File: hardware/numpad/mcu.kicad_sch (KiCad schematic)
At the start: 7 parts, among them U1 STM32L011F4Px

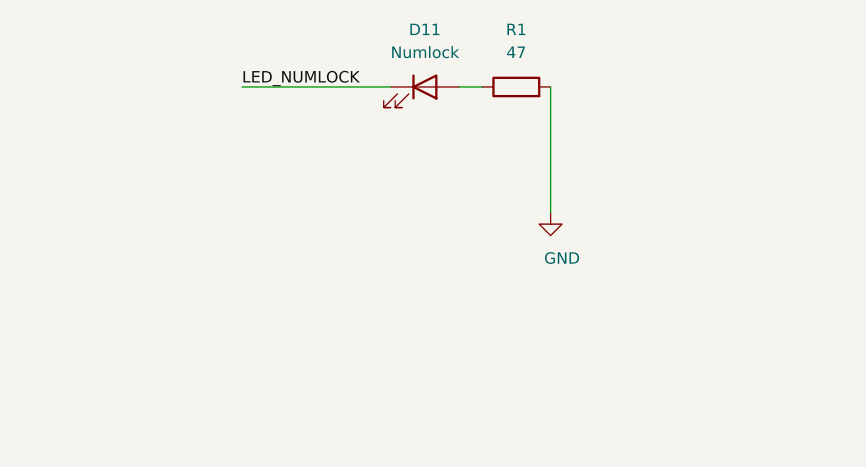
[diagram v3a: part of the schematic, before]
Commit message: Numpad: Add break-away board with the numpad LED
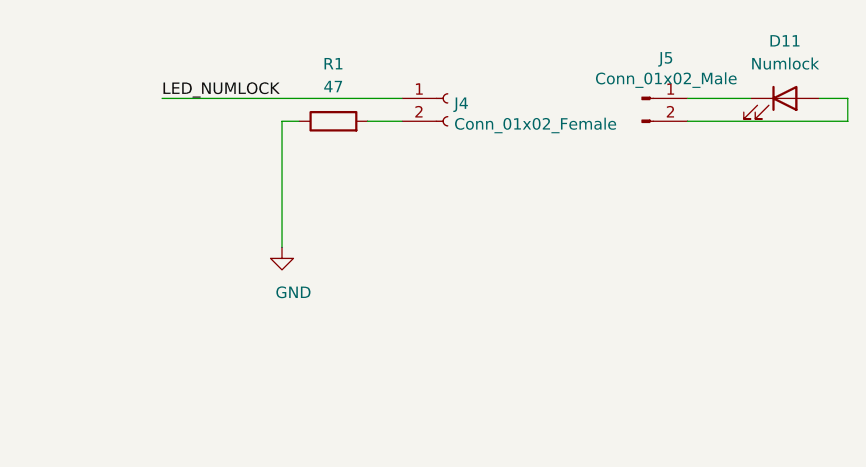
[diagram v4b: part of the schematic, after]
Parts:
- added J4: Conn_01x02_Female, Connector_PinHeader_2.54mm:PinHeader_1x02_P2.54mm_Vertical, symbol Connector:Conn_01x02_Female
- added J5: Conn_01x02_Male, Connector_PinHeader_2.54mm:PinHeader_1x02_P2.54mm_Vertical, symbol Connector:Conn_01x02_Male
- D11: footprint Diode_THT:D_DO-34_SOD68_P2.54mm_Vertical_AnodeUp -> Diode_SMD:D_0603_1608Metric_Pad1.05x0.95mm_HandSolder; Mouser (none) -> 710-150060SS75000; Part Name (none) -> 150060SS75000
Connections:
- net GND: now also R1.1; no longer R1.2
- net LED_NUMLOCK: now also J4.1 (Pin_1); no longer D11.1 (K)
- net at D11.2 (A): now also J5.2 (Pin_2); no longer R1.1
- new net: D11.1 (K), J5.1 (Pin_1)
- new net: J4.2 (Pin_2), R1.2
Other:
- moved on the sheet: D11, R1
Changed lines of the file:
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@@
     (stroke (width 0) (type solid) (color 0 0 0 0))
   )
-  (wire (pts (xy 200.66 54.61) (xy 217.17 54.61))
+  (wire (pts (xy 191.77 55.88) (xy 218.44 55.88))
     (stroke (width 0) (type solid) (color 0 0 0 0))
   )
-  (wire (pts (xy 224.79 54.61) (xy 227.33 54.61))
+  (wire (pts (xy 205.105 58.42) (xy 205.105 72.39))
     (stroke (width 0) (type solid) (color 0 0 0 0))
   )
-  (wire (pts (xy 234.95 54.61) (xy 234.95 68.58))
+  (wire (pts (xy 205.105 58.42) (xy 207.01 58.42))
+    (stroke (width 0) (type solid) (color 0 0 0 0))
+  )
+  (wire (pts (xy 214.63 58.42) (xy 218.44 58.42))
+    (stroke (width 0) (type solid) (color 0 0 0 0))
+  )
+  (wire (pts (xy 250.19 55.88) (xy 257.175 55.88))
+    (stroke (width 0) (type solid) (color 0 0 0 0))
+  )
+  (wire (pts (xy 250.19 58.42) (xy 267.97 58.42))
+    (stroke (width 0) (type solid) (color 0 0 0 0))
+  )
+  (wire (pts (xy 264.795 55.88) (xy 267.97 55.88))
+    (stroke (width 0) (type solid) (color 0 0 0 0))
+  )
+  (wire (pts (xy 267.97 58.42) (xy 267.97 55.88))
     (stroke (width 0) (type solid) (color 0 0 0 0))
   )
@@
     (effects (font (size 1.27 1.27)) (justify right bottom))
   )
-  (label "LED_NUMLOCK" (at 200.66 54.61 0)
+  (label "LED_NUMLOCK" (at 191.77 55.88 0)
     (effects (font (size 1.27 1.27)) (justify left bottom))
   )
@@
     (pin "1")
   )
-  (symbol (lib_id "power:GND") (at 234.95 68.58 0) (unit 1)
+  (symbol (lib_id "power:GND") (at 205.105 72.39 0) (unit 1)
     (in_bom yes) (on_board yes)
-    (property "Reference" "#PWR0112" (id 0) (at 234.95 74.93 0)
+    (property "Reference" "#PWR0112" (id 0) (at 205.105 78.74 0)
       (effects (font (size 1.27 1.27)) hide)
     )
-    (property "Value" "GND" (id 1) (at 236.22 73.66 0))
-    (property "Footprint" "" (id 2) (at 234.95 68.58 0)
+    (property "Value" "GND" (id 1) (at 206.375 77.47 0))
+    (property "Footprint" "" (id 2) (at 205.105 72.39 0)
       (effects (font (size 1.27 1.27)) hide)
     )
-    (property "Datasheet" "" (id 3) (at 234.95 68.58 0)
+    (property "Datasheet" "" (id 3) (at 205.105 72.39 0)
       (effects (font (size 1.27 1.27)) hide)
     )
     (pin "1")
   )
-  (symbol (lib_id "Device:R") (at 231.14 54.61 90) (unit 1)
+  (symbol (lib_id "Device:R") (at 210.82 58.42 90) (unit 1)
     (in_bom yes) (on_board yes)
-    (property "Reference" "R1" (id 0) (at 231.14 48.26 90))
-    (property "Value" "47" (id 1) (at 231.14 50.8 90))
-    (property "Footprint" "Resistor_SMD:R_0603_1608Metric_Pad0.98x0.95mm_HandSolder" (id 2) (at 231.14 56.388 90)
+    (property "Reference" "R1" (id 0) (at 210.82 52.07 90))
+    (property "Value" "47" (id 1) (at 210.82 54.61 90))
+    (property "Footprint" "Resistor_SMD:R_0603_1608Metric_Pad0.98x0.95mm_HandSolder" (id 2) (at 210.82 60.198 90)
       (effects (font (size 1.27 1.27)) hide)
     )
-    (property "Datasheet" "~" (id 3) (at 231.14 54.61 0)
+    (property "Datasheet" "~" (id 3) (at 210.82 58.42 0)
       (effects (font (size 1.27 1.27)) hide)
     )
@@
     (pin "2")
   )
-  (symbol (lib_id "Device:LED") (at 220.98 54.61 0) (unit 1)
+  (symbol (lib_id "Connector:Conn_01x02_Male") (at 245.11 55.88 0) (unit 1)
     (in_bom yes) (on_board yes)
-    (property "Reference" "D11" (id 0) (at 220.98 48.26 0))
-    (property "Value" "Numlock" (id 1) (at 220.98 50.8 0))
-    (property "Footprint" "Diode_THT:D_DO-34_SOD68_P2.54mm_Vertical_AnodeUp" (id 2) (at 220.98 54.61 0)
+    (property "Reference" "J5" (id 0) (at 247.8024 51.4158 0))
+    (property "Value" "Conn_01x02_Male" (id 1) (at 247.8024 53.7145 0))
+    (property "Footprint" "Connector_PinHeader_2.54mm:PinHeader_1x02_P2.54mm_Vertical" (id 2) (at 245.11 55.88 0)
       (effects (font (size 1.27 1.27)) hide)
     )
-    (property "Datasheet" "~" (id 3) (at 220.98 54.61 0)
+    (property "Datasheet" "~" (id 3) (at 245.11 55.88 0)
       (effects (font (size 1.27 1.27)) hide)
     )
+    (pin "1")
+    (pin "2")
+  )
+  (symbol (lib_id "Connector:Conn_01x02_Female") (at 223.52 55.88 0) (unit 1)
+    (in_bom yes) (on_board yes)
+    (property "Reference" "J4" (id 0) (at 224.2313 56.4578 0)
+      (effects (font (size 1.27 1.27)) (justify left))
+    )
+    (property "Value" "Conn_01x02_Female" (id 1) (at 224.2313 58.7565 0)
+      (effects (font (size 1.27 1.27)) (justify left))
+    )
+    (property "Footprint" "Connector_PinHeader_2.54mm:PinHeader_1x02_P2.54mm_Vertical" (id 2) (at 223.52 55.88 0)
+      (effects (font (size 1.27 1.27)) hide)
+    )
+    (property "Datasheet" "~" (id 3) (at 223.52 55.88 0)
+      (effects (font (size 1.27 1.27)) hide)
+    )
+    (pin "1")
+    (pin "2")
+  )
+  (symbol (lib_id "Device:LED") (at 260.985 55.88 0) (unit 1)
+    (in_bom yes) (on_board yes)
+    (property "Reference" "D11" (id 0) (at 260.985 49.53 0))
+    (property "Value" "Numlock" (id 1) (at 260.985 52.07 0))
+    (property "Footprint" "Diode_SMD:D_0603_1608Metric_Pad1.05x0.95mm_HandSolder" (id 2) (at 260.985 55.88 0)
+      (effects (font (size 1.27 1.27)) hide)
+    )
+    (property "Datasheet" "~" (id 3) (at 260.985 55.88 0)
+      (effects (font (size 1.27 1.27)) hide)
+    )
+    (property "Mouser" "710-150060SS75000" (id 4) (at 260.985 55.88 0)
+      (effects (font (size 1.27 1.27)) hide)
+    )
+    (property "Part Name" "150060SS75000 " (id 5) (at 260.985 55.88 0)
+      (effects (font (size 1.27 1.27)) hide)
+    )

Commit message: Numpad: Exchange footprint of the numpad-LED connection
The 2.54 mm pin-header did not fit between the switches as the
silkscreens overlapped.
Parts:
- J4, J5: footprint Connector_PinHeader_2.54mm:PinHeader_1x02_P2.54mm_Vertical -> Connector_PinSocket_2.00mm:PinSocket_1x02_P2.00mm_Vertical
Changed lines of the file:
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@@
     (property "Reference" "J5" (id 0) (at 247.8024 51.4158 0))
     (property "Value" "Conn_01x02_Male" (id 1) (at 247.8024 53.7145 0))
-    (property "Footprint" "Connector_PinHeader_2.54mm:PinHeader_1x02_P2.54mm_Vertical" (id 2) (at 245.11 55.88 0)
+    (property "Footprint" "Connector_PinSocket_2.00mm:PinSocket_1x02_P2.00mm_Vertical" (id 2) (at 245.11 55.88 0)
       (effects (font (size 1.27 1.27)) hide)
     )
@@
       (effects (font (size 1.27 1.27)) (justify left))
     )
-    (property "Footprint" "Connector_PinHeader_2.54mm:PinHeader_1x02_P2.54mm_Vertical" (id 2) (at 223.52 55.88 0)
+    (property "Footprint" "Connector_PinSocket_2.00mm:PinSocket_1x02_P2.00mm_Vertical" (id 2) (at 223.52 55.88 0)
       (effects (font (size 1.27 1.27)) hide)
     )

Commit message: Numpad: Add missing part numbers
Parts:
- C2, C4: Mouser (none) -> 581-06033C104KAT4A; Part Name (none) -> AVX 06033C104KAT4A
- C3, C5: footprint Capacitor_SMD:C_0603_1608Metric_Pad1.08x0.95mm_HandSolder -> Capacitor_SMD:C_0805_2012Metric; Mouser (none) -> 187-CL21A106KOQNNNG; Part Name (none) -> Samsung CL21A106KOQNNNG
- J4, J5: Mouser (none) -> -; Part Name (none) -> -
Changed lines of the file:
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@@
+      (effects (font (size 1.27 1.27)) hide)
+    )
+    (property "Mouser" "-" (id 4) (at 245.11 55.88 0)
+      (effects (font (size 1.27 1.27)) hide)
+    )
+    (property "Part Name" "-" (id 5) (at 245.11 55.88 0)
       (effects (font (size 1.27 1.27)) hide)
     )
@@
     )
     (property "Datasheet" "~" (id 3) (at 223.52 55.88 0)
+      (effects (font (size 1.27 1.27)) hide)
+    )
+    (property "Mouser" "-" (id 4) (at 223.52 55.88 0)
+      (effects (font (size 1.27 1.27)) hide)
+    )
+    (property "Part Name" "-" (id 5) (at 223.52 55.88 0)
       (effects (font (size 1.27 1.27)) hide)
     )
@@
       (effects (font (size 1.27 1.27)) hide)
     )
+    (property "Mouser" "581-06033C104KAT4A" (id 4) (at 80.01 73.66 0)
+      (effects (font (size 1.27 1.27)) hide)
+    )
+    (property "Part Name" "AVX 06033C104KAT4A " (id 5) (at 80.01 73.66 0)
+      (effects (font (size 1.27 1.27)) hide)
+    )
     (pin "1")
     (pin "2")
@@
       (effects (font (size 1.27 1.27)) (justify left))
     )
-    (property "Footprint" "Capacitor_SMD:C_0603_1608Metric_Pad1.08x0.95mm_HandSolder" (id 2) (at 93.6752 77.47 0)
+    (property "Footprint" "Capacitor_SMD:C_0805_2012Metric" (id 2) (at 93.6752 77.47 0)
       (effects (font (size 1.27 1.27)) hide)
     )
     (property "Datasheet" "~" (id 3) (at 92.71 73.66 0)
+      (effects (font (size 1.27 1.27)) hide)
+    )
+    (property "Mouser" "187-CL21A106KOQNNNG" (id 4) (at 92.71 73.66 0)
+      (effects (font (size 1.27 1.27)) hide)
+    )
+    (property "Part Name" "Samsung CL21A106KOQNNNG" (id 5) (at 92.71 73.66 0)
       (effects (font (size 1.27 1.27)) hide)
     )
@@
       (effects (font (size 1.27 1.27)) hide)
     )
+    (property "Mouser" "581-06033C104KAT4A" (id 4) (at 110.49 73.66 0)
+      (effects (font (size 1.27 1.27)) hide)
+    )
+    (property "Part Name" "AVX 06033C104KAT4A " (id 5) (at 110.49 73.66 0)
+      (effects (font (size 1.27 1.27)) hide)
+    )
     (pin "1")
     (pin "2")
@@
       (effects (font (size 1.27 1.27)) (justify left))
     )
-    (property "Footprint" "Capacitor_SMD:C_0603_1608Metric_Pad1.08x0.95mm_HandSolder" (id 2) (at 124.1552 77.47 0)
+    (property "Footprint" "Capacitor_SMD:C_0805_2012Metric" (id 2) (at 124.1552 77.47 0)
       (effects (font (size 1.27 1.27)) hide)
     )
@@
       (effects (font (size 1.27 1.27)) hide)
     )
+    (property "Mouser" "187-CL21A106KOQNNNG" (id 4) (at 123.19 73.66 0)
+      (effects (font (size 1.27 1.27)) hide)
+    )
+    (property "Part Name" "Samsung CL21A106KOQNNNG" (id 5) (at 123.19 73.66 0)
+      (effects (font (size 1.27 1.27)) hide)
+    )

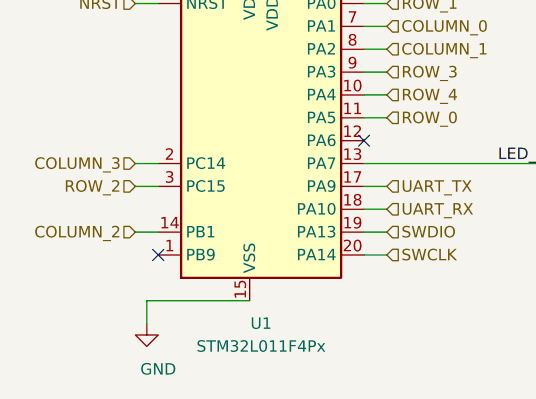
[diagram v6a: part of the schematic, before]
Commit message: Numpad: Add pullup for reset and connect BOOT0 to ground
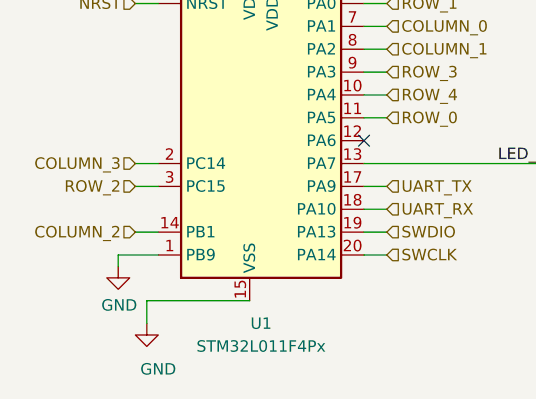
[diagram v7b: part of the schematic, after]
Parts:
- U1: Mouser 511-STM32L011F4P6 -> 511-STM32L011F4P6
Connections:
- net GND: now also U1.1 (PB9)
- no-connect marks 2 -> 1
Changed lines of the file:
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@@
   (junction (at 110.49 66.04) (diameter 0.9144) (color 0 0 0 0))
   (junction (at 110.49 81.28) (diameter 0.9144) (color 0 0 0 0))
-  (no_connect (at 91.44 118.11))
   (no_connect (at 114.3 105.41))
   (wire (pts (xy 80.01 66.04) (xy 80.01 69.85))
@@
     (stroke (width 0) (type solid) (color 0 0 0 0))
   )
+  (wire (pts (xy 86.995 118.11) (xy 91.44 118.11))
+    (stroke (width 0) (type solid) (color 0 0 0 0))
+  )
+  (wire (pts (xy 86.995 119.38) (xy 86.995 118.11))
+    (stroke (width 0) (type solid) (color 0 0 0 0))
+  )
   (wire (pts (xy 88.9 90.17) (xy 91.44 90.17))
     (stroke (width 0) (type solid) (color 0 0 0 0))
@@
     )
     (property "Datasheet" "" (id 3) (at 102.87 81.28 0)
+      (effects (font (size 1.27 1.27)) hide)
+    )
+    (pin "1")
+  )
+  (symbol (lib_id "power:GND") (at 86.995 119.38 0) (unit 1)
+    (in_bom yes) (on_board yes)
+    (property "Reference" "#PWR?" (id 0) (at 86.995 125.73 0)
+      (effects (font (size 1.27 1.27)) hide)
+    )
+    (property "Value" "GND" (id 1) (at 87.1093 123.7044 0))
+    (property "Footprint" "" (id 2) (at 86.995 119.38 0)
+      (effects (font (size 1.27 1.27)) hide)
+    )
+    (property "Datasheet" "" (id 3) (at 86.995 119.38 0)
       (effects (font (size 1.27 1.27)) hide)
     )
@@
       (effects (font (size 1.27 1.27)) hide)
     )
-    (property "Mouser" " 511-STM32L011F4P6 " (id 4) (at 104.14 102.87 0)
-      (effects (font (size 1.27 1.27)) hide)
-    )
+    (property "Mouser" "511-STM32L011F4P6 " (id 4) (at 104.14 102.87 0)
+      (effects (font (size 1.27 1.27)) hide)
+    )

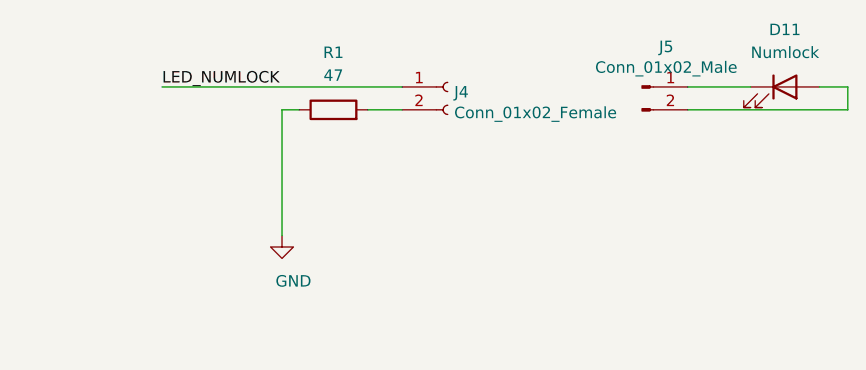
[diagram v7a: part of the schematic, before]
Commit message: Numpad: Connect the break-away-board to the main with traces
This allows software development without having to solder the LED to the
PCB with wires.
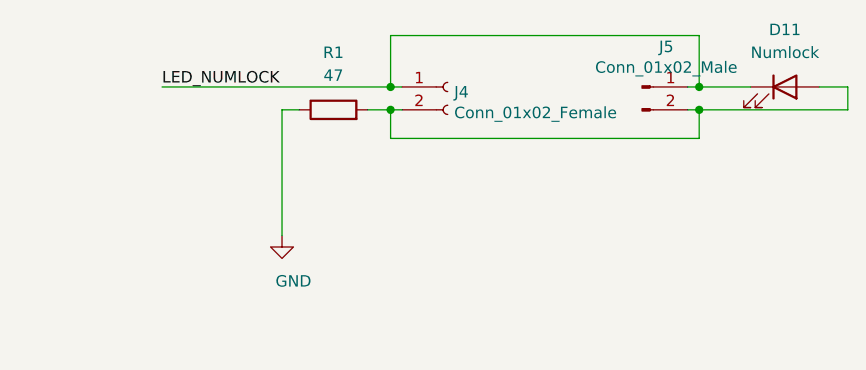
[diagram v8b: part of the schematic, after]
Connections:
- net LED_NUMLOCK: now also D11.1 (K), J5.1 (Pin_1)
- net at D11.2 (A), J5.2 (Pin_2): now also J4.2 (Pin_2), R1.2
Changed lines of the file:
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@@
   (junction (at 110.49 66.04) (diameter 0.9144) (color 0 0 0 0))
   (junction (at 110.49 81.28) (diameter 0.9144) (color 0 0 0 0))
+  (junction (at 217.17 55.88) (diameter 0.9144) (color 0 0 0 0))
+  (junction (at 217.17 58.42) (diameter 0.9144) (color 0 0 0 0))
+  (junction (at 251.46 55.88) (diameter 0.9144) (color 0 0 0 0))
+  (junction (at 251.46 58.42) (diameter 0.9144) (color 0 0 0 0))
   (no_connect (at 114.3 105.41))
   (wire (pts (xy 80.01 66.04) (xy 80.01 69.85))
@@
     (stroke (width 0) (type solid) (color 0 0 0 0))
   )
-  (wire (pts (xy 191.77 55.88) (xy 218.44 55.88))
+  (wire (pts (xy 191.77 55.88) (xy 217.17 55.88))
     (stroke (width 0) (type solid) (color 0 0 0 0))
   )
@@
     (stroke (width 0) (type solid) (color 0 0 0 0))
   )
-  (wire (pts (xy 214.63 58.42) (xy 218.44 58.42))
-    (stroke (width 0) (type solid) (color 0 0 0 0))
-  )
-  (wire (pts (xy 250.19 55.88) (xy 257.175 55.88))
-    (stroke (width 0) (type solid) (color 0 0 0 0))
-  )
-  (wire (pts (xy 250.19 58.42) (xy 267.97 58.42))
+  (wire (pts (xy 214.63 58.42) (xy 217.17 58.42))
+    (stroke (width 0) (type solid) (color 0 0 0 0))
+  )
+  (wire (pts (xy 217.17 50.165) (xy 251.46 50.165))
+    (stroke (width 0) (type solid) (color 0 0 0 0))
+  )
+  (wire (pts (xy 217.17 55.88) (xy 217.17 50.165))
+    (stroke (width 0) (type solid) (color 0 0 0 0))
+  )
+  (wire (pts (xy 217.17 55.88) (xy 218.44 55.88))
+    (stroke (width 0) (type solid) (color 0 0 0 0))
+  )
+  (wire (pts (xy 217.17 58.42) (xy 218.44 58.42))
+    (stroke (width 0) (type solid) (color 0 0 0 0))
+  )
+  (wire (pts (xy 217.17 61.595) (xy 217.17 58.42))
+    (stroke (width 0) (type solid) (color 0 0 0 0))
+  )
+  (wire (pts (xy 250.19 55.88) (xy 251.46 55.88))
+    (stroke (width 0) (type solid) (color 0 0 0 0))
+  )
+  (wire (pts (xy 250.19 58.42) (xy 251.46 58.42))
+    (stroke (width 0) (type solid) (color 0 0 0 0))
+  )
+  (wire (pts (xy 251.46 50.165) (xy 251.46 55.88))
+    (stroke (width 0) (type solid) (color 0 0 0 0))
+  )
+  (wire (pts (xy 251.46 55.88) (xy 257.175 55.88))
+    (stroke (width 0) (type solid) (color 0 0 0 0))
+  )
+  (wire (pts (xy 251.46 58.42) (xy 251.46 61.595))
+    (stroke (width 0) (type solid) (color 0 0 0 0))
+  )
+  (wire (pts (xy 251.46 58.42) (xy 267.97 58.42))
+    (stroke (width 0) (type solid) (color 0 0 0 0))
+  )
+  (wire (pts (xy 251.46 61.595) (xy 217.17 61.595))
     (stroke (width 0) (type solid) (color 0 0 0 0))
   )
@@
   (symbol (lib_id "power:GND") (at 86.995 119.38 0) (unit 1)
     (in_bom yes) (on_board yes)
-    (property "Reference" "#PWR?" (id 0) (at 86.995 125.73 0)
-      (effects (font (size 1.27 1.27)) hide)
-    )
+    (property "Reference" "#PWR0116" (id 0) (at 86.995 125.73 0)
+      (effects (font (size 1.27 1.27)) hide)
+    )
